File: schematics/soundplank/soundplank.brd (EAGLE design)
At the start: 50 x 49 mm, 20 parts, among them IC1 74AHC1G86DBV

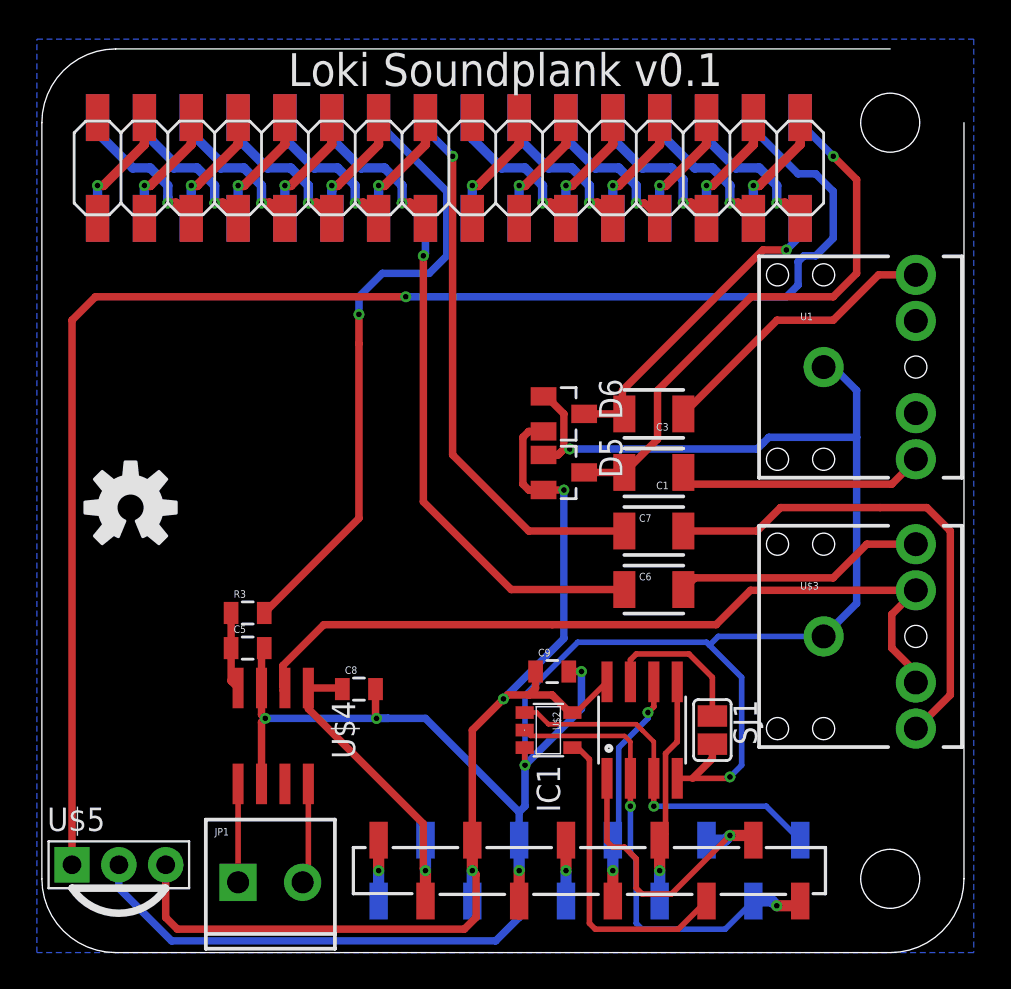
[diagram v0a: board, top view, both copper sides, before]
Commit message: Improved soundplank labelling; generated gerbers.
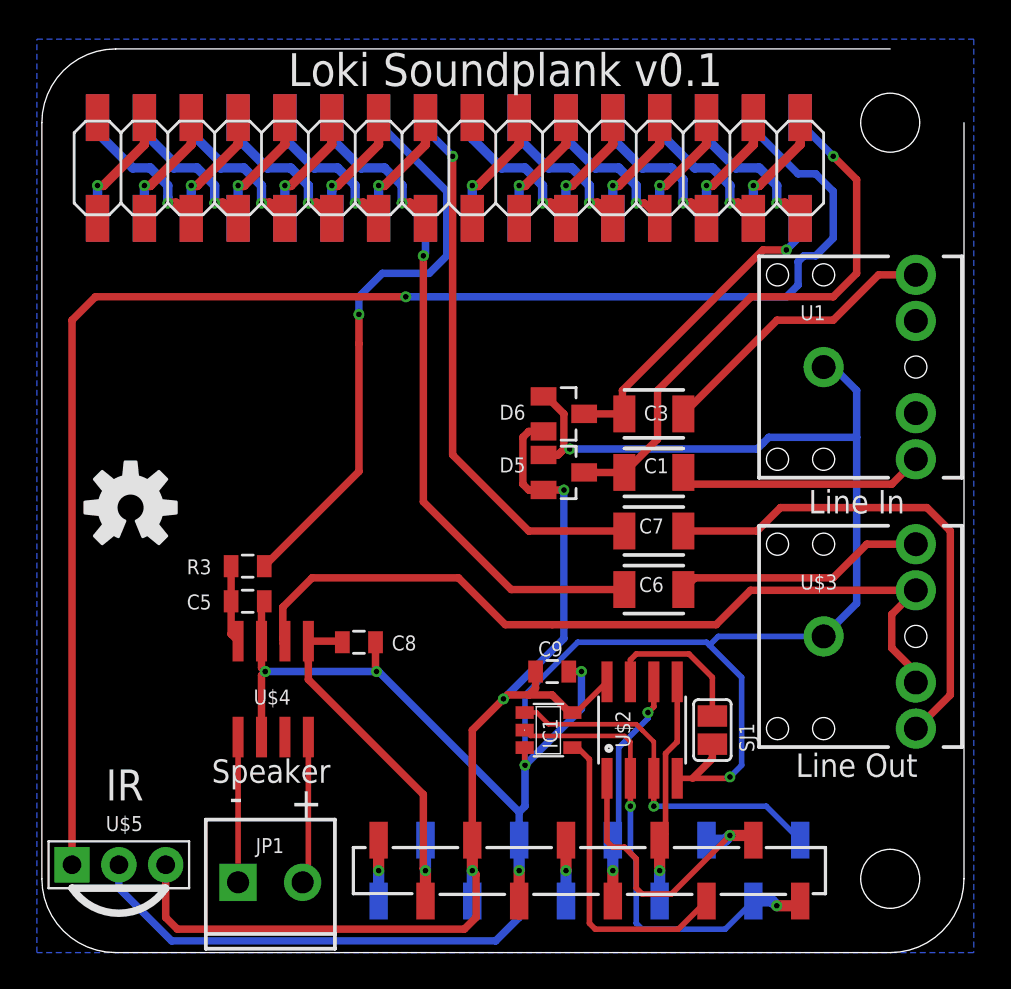
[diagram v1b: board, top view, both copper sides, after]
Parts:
- moved C8 2.54 mm to (17.5, 16.8)
- moved C5 2.54 mm to (11.4, 19.1)
- moved R3 2.54 mm to (11.4, 21.0)
- moved U$4 2.54 mm to (12.8, 14.3)
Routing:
- net +5V: track 17.7 -> 20.4 mm
- net VOL: track 34.0 -> 31.4 mm
- net N$33: track 5.34 -> 7.88 mm
- net N$30: track 5.47 -> 8.01 mm
- net N$38: track 43.5 -> 45.1 mm
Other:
- board text added: "+"
- board text added: "-"
- board text added: "IR"
- board text added: "Line In"
- board text added: "Line Out"
- board text added: "Speaker"

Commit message: Updated soundplank to make use of opamp outputs when on the bottom.
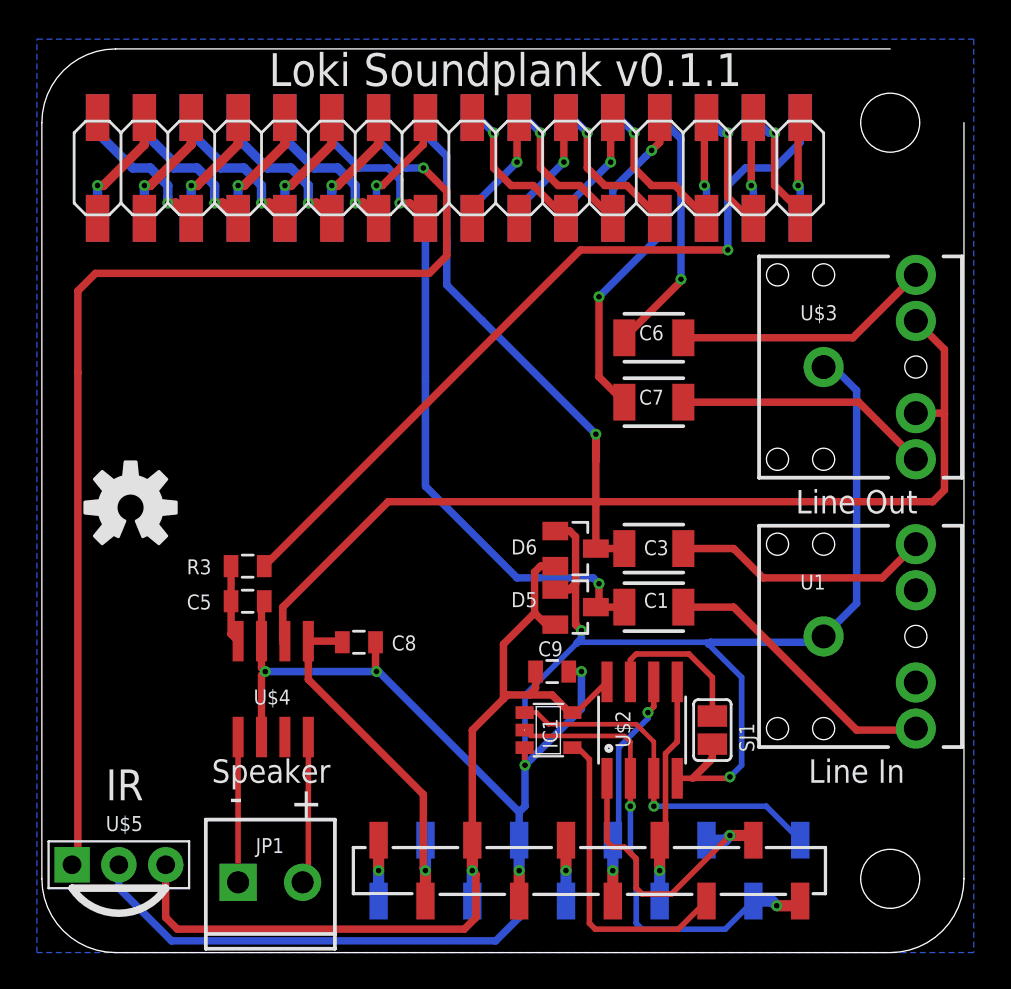
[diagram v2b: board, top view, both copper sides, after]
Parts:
- moved U$3 14.6 mm to (42.7, 31.8)
- moved U1 14.6 mm to (42.7, 17.1)
- moved C6 13.7 mm to (33.5, 33.3)
- moved D6 7.33 mm to (29.2, 21.9)
- moved D5 7.33 mm to (29.2, 18.7)
- moved C3 7.30 mm to (33.5, 21.9)
- moved C1 7.30 mm to (33.5, 18.7)
- moved C7 6.98 mm to (33.5, 29.8)
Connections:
- removed net N$10 (its old number): U$1.I1.7, U$1.O1.4
- removed net N$11 (its old number): U$1.I1.6, U$1.O1.3
- removed net N$12 (its old number): U$1.I1.5, U$1.O1.2
- removed net N$13 (its old number): U$1.I1.4, U$1.O1.1
- removed net N$9 (its old number): U$1.I1.8, U$1.O1.5
- new net N$1: U$1.I1.2, U$1.O1.1
- new net N$2: U$1.I1.3, U$1.O1.2
- new net N$3: U$1.I1.4, U$1.O1.3
- new net N$4: U$1.I1.5, U$1.O1.4
- new net N$5: U$1.I1.6, U$1.O1.5
- net INL: now also U$1.I2.2; no longer U$1.I1.1
- net INR: now also U$1.I2.1; no longer U$1.I1.2
- net IR: now also U$1.I2.3; no longer U$1.I1.3
- net OUTL: now also U$1.I1.8; no longer U$1.I2.1
- net OUTR: now also U$1.I1.7; no longer U$1.I2.2
- net VOL: now also U$1.I1.1; no longer U$1.I2.3
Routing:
- net IR: track 82.3 -> 61.6 mm
- net OUTL: track 30.1 -> 11.9 mm
- net OUTR: track 28.3 -> 13.7 mm
- net INR: track 17.6 -> 30.8 mm
- net LINEL: track 27.0 -> 13.9 mm
- net GND: track 142.1 -> 129.9 mm
- net VOL: track 31.4 -> 42.0 mm
- net +3V3: track 61.5 -> 52.9 mm, vias 3 -> 1
- net N$12 (its old number): track 8.57 -> 0.00 mm, vias 1 -> 0
- net N$10 (its old number): track 8.38 -> 0.00 mm, vias 1 -> 0
- net N$38: track 45.1 -> 52.3 mm
- net N$4: track 0.00 -> 6.85 mm, vias 0 -> 1
- net N$2: track 0.00 -> 6.71 mm, vias 0 -> 1
- net N$9 (its old number): track 6.70 -> 0.00 mm, vias 1 -> 0
- net N$13 (its old number): track 6.70 -> 0.00 mm, vias 1 -> 0
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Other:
- board text added: "Loki Soundplank v0.1.1"
- board text removed: "Loki Soundplank v0.1"

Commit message: Fix footprints on the soundplank so they're not backwards (oops!)
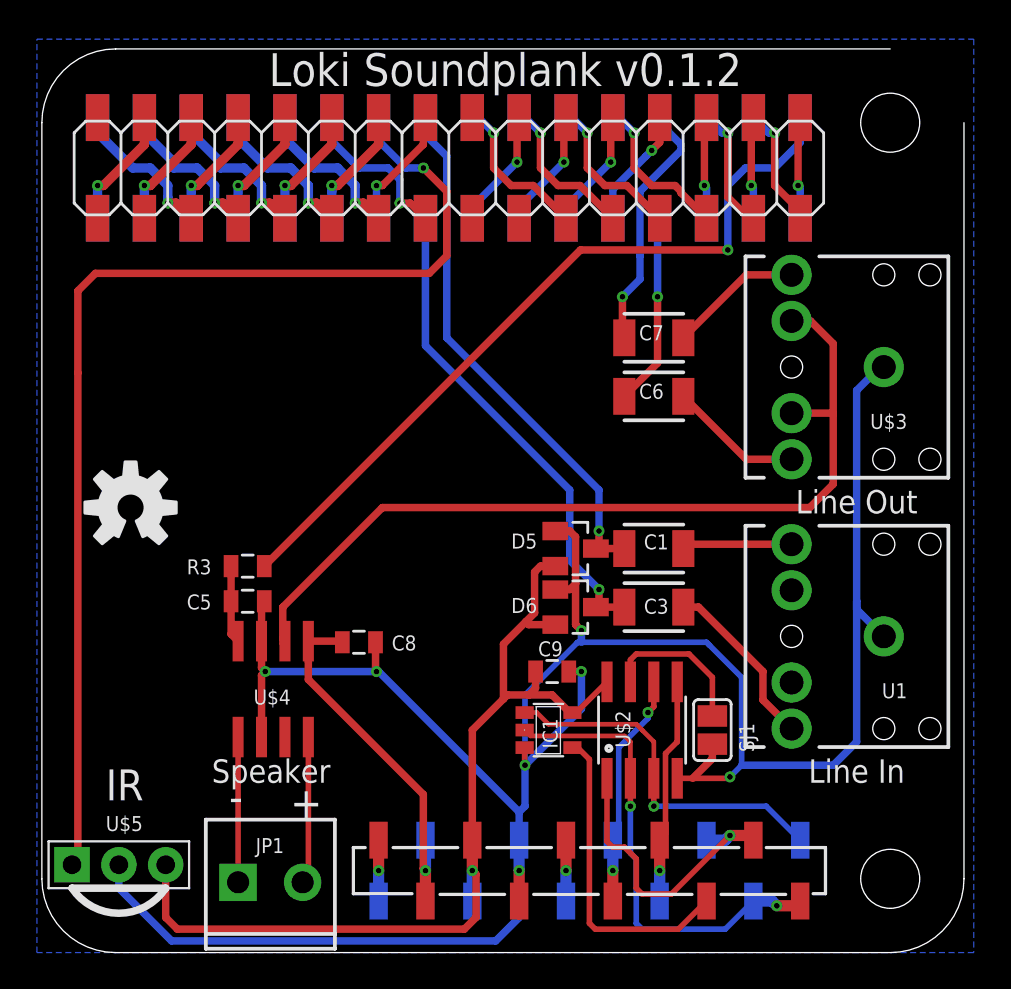
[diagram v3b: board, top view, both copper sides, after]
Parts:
- moved C7 3.49 mm to (33.5, 33.3)
- moved U$3 3.26 mm to (45.9, 31.8), turned to 180 degrees
- moved U1 3.26 mm to (45.9, 17.1), turned to 180 degrees
- moved C1 3.17 mm to (33.5, 21.9)
- moved C3 3.17 mm to (33.5, 18.7)
- moved C6 3.17 mm to (33.5, 30.2)
- moved D5 3.17 mm to (29.2, 21.9)
- moved D6 3.17 mm to (29.2, 18.7)
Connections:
- net INL: now also U$1.I2.1; no longer U$1.I2.2
- net INR: now also U$1.I2.2; no longer U$1.I2.1
- net OUTL: now also U$1.I1.7; no longer U$1.I1.8
- net OUTR: now also U$1.I1.8; no longer U$1.I1.7
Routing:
- net N$34: track 15.4 -> 5.97 mm
- net GND: track 129.9 -> 136.8 mm
- net LINER: track 14.0 -> 7.28 mm
- net LINEL: track 13.9 -> 7.28 mm
- net N$38: track 52.3 -> 47.6 mm
- net N$39: track 14.0 -> 9.50 mm
- net INR: track 30.8 -> 26.6 mm
- net OUTR: track 13.7 -> 10.4 mm
- net OUTL: track 11.9 -> 13.8 mm
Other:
- board text added: "Loki Soundplank v0.1.2"
- board text removed: "Loki Soundplank v0.1.1"

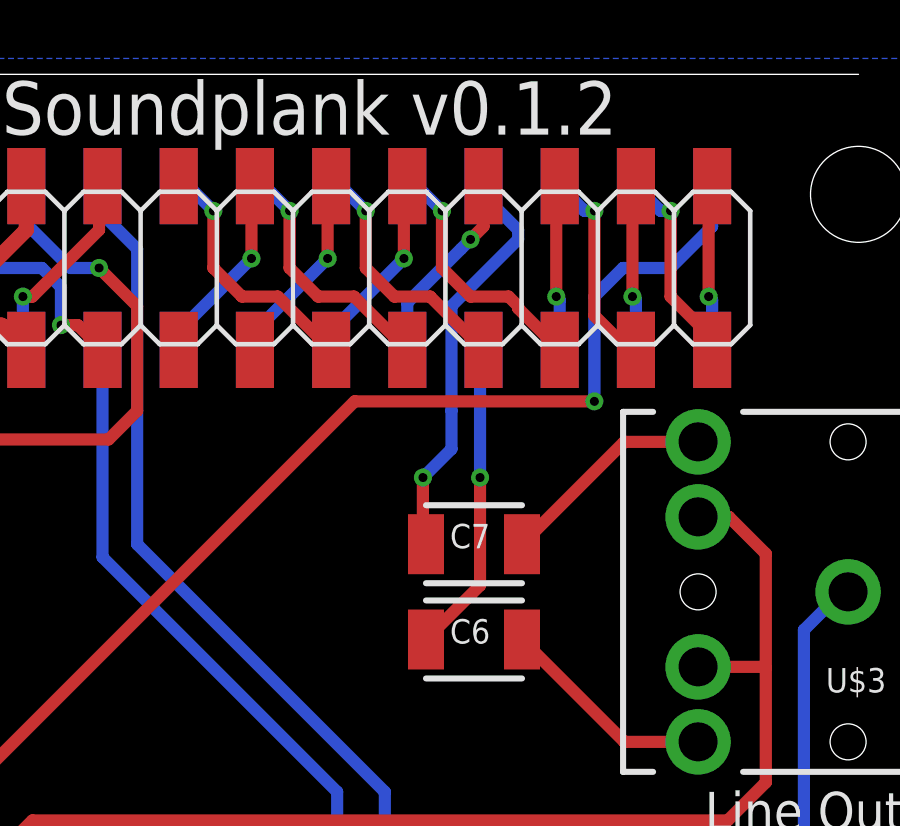
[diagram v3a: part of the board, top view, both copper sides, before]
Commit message: Improve audio routing for line out.
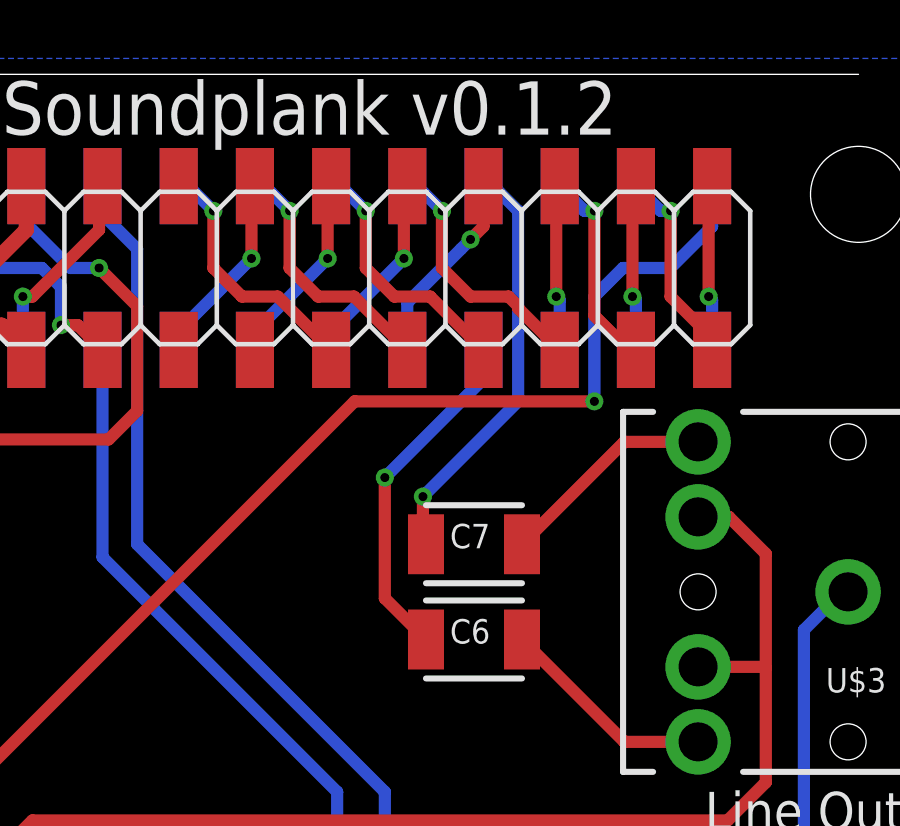
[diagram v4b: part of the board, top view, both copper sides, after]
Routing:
- net OUTR: track 10.4 -> 11.6 mm
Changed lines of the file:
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@@
 <contactref element="C7" pad="1"/>
 <contactref element="U$1" pad="I1.7"/>
-<wire x1="33.77" y1="45.275" x2="33.77" y2="44.97" width="0.4064" layer="16"/>
-<wire x1="33.77" y1="44.97" x2="34.925" y2="43.815" width="0.4064" layer="16"/>
-<wire x1="34.925" y1="43.815" x2="34.925" y2="43.4975" width="0.4064" layer="16"/>
-<wire x1="34.925" y1="43.4975" x2="32.7025" y2="41.275" width="0.4064" layer="16"/>
-<wire x1="32.7025" y1="41.275" x2="32.7025" y2="37.7825" width="0.4064" layer="16"/>
-<wire x1="32.7025" y1="37.7825" x2="32.7025" y2="36.5125" width="0.4064" layer="16"/>
-<wire x1="32.7025" y1="36.5125" x2="31.75" y2="35.56" width="0.4064" layer="16"/>
-<via x="31.75" y="35.56" extent="1-16" drill="0.3"/>
-<wire x1="31.75" y1="35.56" x2="31.75" y2="33.44" width="0.4064" layer="1"/>
+<wire x1="33.77" y1="45.275" x2="34.1" y2="45.275" width="0.4064" layer="16"/>
+<wire x1="34.1" y1="45.275" x2="34.925" y2="44.45" width="0.4064" layer="16"/>
+<wire x1="34.925" y1="44.45" x2="34.925" y2="38.1" width="0.4064" layer="16"/>
+<wire x1="34.925" y1="38.1" x2="31.75" y2="34.925" width="0.4064" layer="16"/>
+<via x="31.75" y="34.925" extent="1-16" drill="0.3"/>
+<wire x1="31.75" y1="34.925" x2="31.75" y2="33.44" width="0.4064" layer="1"/>
 <wire x1="31.75" y1="33.44" x2="31.8525" y2="33.3375" width="0.4064" layer="1"/>
 </signal>
@@
 <contactref element="C6" pad="1"/>
 <contactref element="U$1" pad="I1.8"/>
-<wire x1="33.655" y1="35.56" x2="33.655" y2="39.7" width="0.4064" layer="16"/>
-<wire x1="33.655" y1="39.7" x2="33.77" y2="39.815" width="0.4064" layer="16"/>
-<via x="33.655" y="35.56" extent="1-16" drill="0.3"/>
-<wire x1="33.655" y1="35.56" x2="33.655" y2="31.965" width="0.4064" layer="1"/>
-<wire x1="33.655" y1="31.965" x2="31.8525" y2="30.1625" width="0.4064" layer="1"/>
+<wire x1="33.77" y1="39.815" x2="33.77" y2="38.85" width="0.4064" layer="16"/>
+<wire x1="33.77" y1="38.85" x2="30.48" y2="35.56" width="0.4064" layer="16"/>
+<via x="30.48" y="35.56" extent="1-16" drill="0.3"/>
+<wire x1="30.48" y1="35.56" x2="30.48" y2="31.535" width="0.4064" layer="1"/>
+<wire x1="30.48" y1="31.535" x2="31.8525" y2="30.1625" width="0.4064" layer="1"/>
 </signal>
 <signal name="VOL">

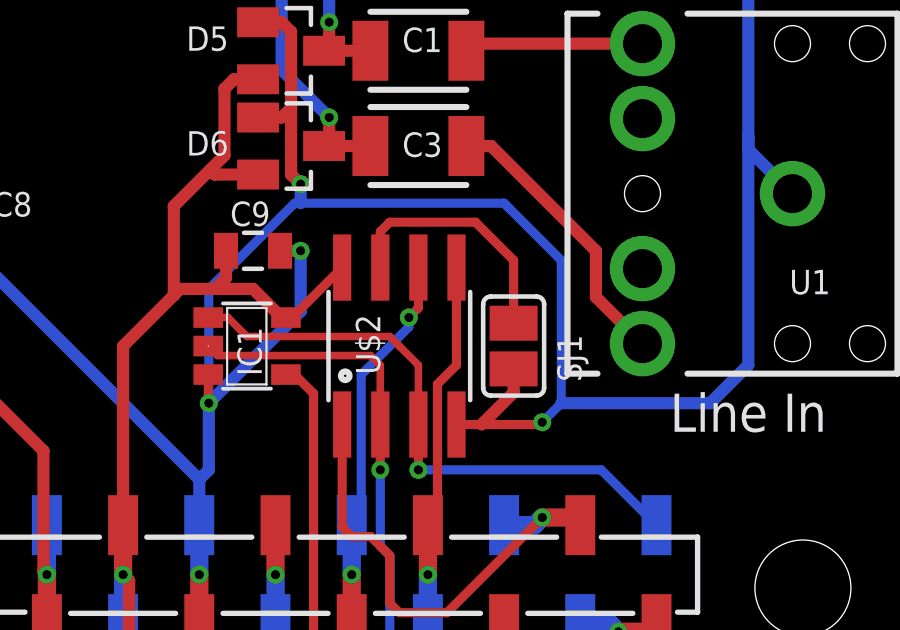
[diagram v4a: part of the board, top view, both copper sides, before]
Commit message: Fix write protect pullups on plank EEPROMs.
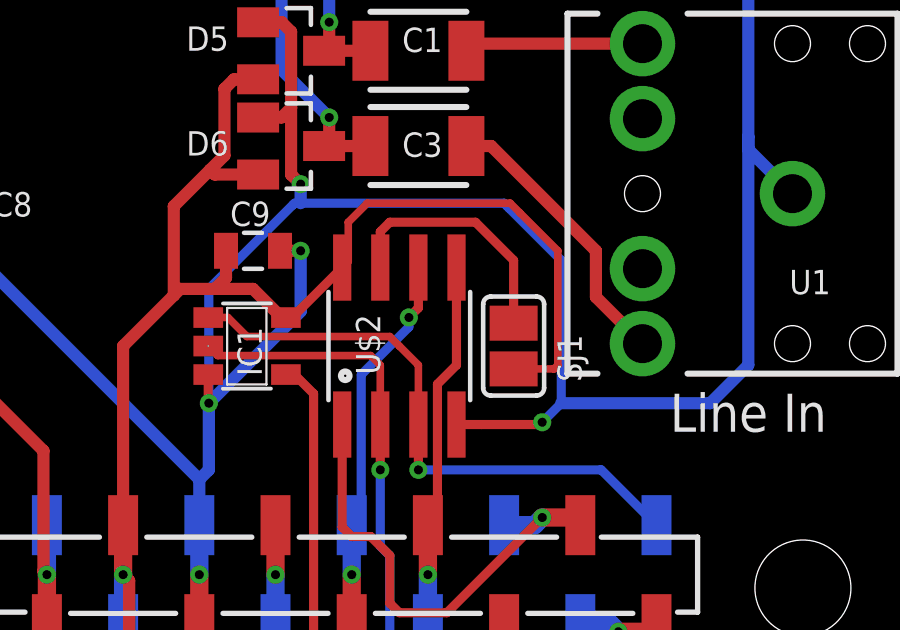
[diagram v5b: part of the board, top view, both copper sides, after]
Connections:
- net +3V3: now also SJ1.2
- net GND: no longer SJ1.2
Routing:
- net +3V3: track 53.2 -> 68.0 mm
- net GND: track 136.8 -> 134.5 mm
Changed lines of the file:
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@@
 <wire x1="28.11" y1="17.7825" x2="26.6675" y2="17.7825" width="0.4064" layer="1"/>
 <wire x1="26.6675" y1="17.7825" x2="26.51125" y2="17.93875" width="0.4064" layer="1"/>
+<contactref element="SJ1" pad="2"/>
+<wire x1="36.6275" y1="11.303" x2="37.973" y2="11.303" width="0.254" layer="1"/>
+<wire x1="37.973" y1="11.303" x2="38.1" y2="11.43" width="0.254" layer="1"/>
+<wire x1="38.1" y1="11.43" x2="38.1" y2="15.24" width="0.254" layer="1"/>
+<wire x1="38.1" y1="15.24" x2="36.83" y2="16.51" width="0.254" layer="1"/>
+<wire x1="36.83" y1="16.51" x2="36.5125" y2="16.8275" width="0.254" layer="1"/>
+<wire x1="36.5125" y1="16.8275" x2="31.75" y2="16.8275" width="0.254" layer="1"/>
+<wire x1="31.75" y1="16.8275" x2="31.115" y2="16.1925" width="0.254" layer="1"/>
+<wire x1="31.115" y1="16.1925" x2="31.115" y2="14.8837" width="0.254" layer="1"/>
+<wire x1="31.115" y1="14.8837" x2="30.9125" y2="14.6812" width="0.254" layer="1"/>
 </signal>
 <signal name="GND">
@@
 <contactref element="IC1" pad="3"/>
 <contactref element="U$2" pad="4"/>
-<contactref element="SJ1" pad="2"/>
 <wire x1="26.15" y1="6.095" x2="26.15" y2="4.445" width="0.6096" layer="16"/>
 <via x="26.15" y="4.445" extent="1-16" drill="0.3"/>
@@
 <wire x1="12.18" y1="11.6875" x2="12.18" y2="15.0375" width="0.4064" layer="1"/>
 <wire x1="12.18" y1="15.0375" x2="12.3825" y2="15.24" width="0.4064" layer="1"/>
-<wire x1="36.6275" y1="11.303" x2="36.6275" y2="10.5163" width="0.4064" layer="1"/>
-<wire x1="36.6275" y1="10.5163" x2="35.56" y2="9.4488" width="0.4064" layer="1"/>
 <polygon width="0.4064" layer="16">
 <vertex x="0" y="0"/>
